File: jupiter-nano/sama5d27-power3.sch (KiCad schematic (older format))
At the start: 25 parts, among them U3 MIC5247-2.0YM5-TR

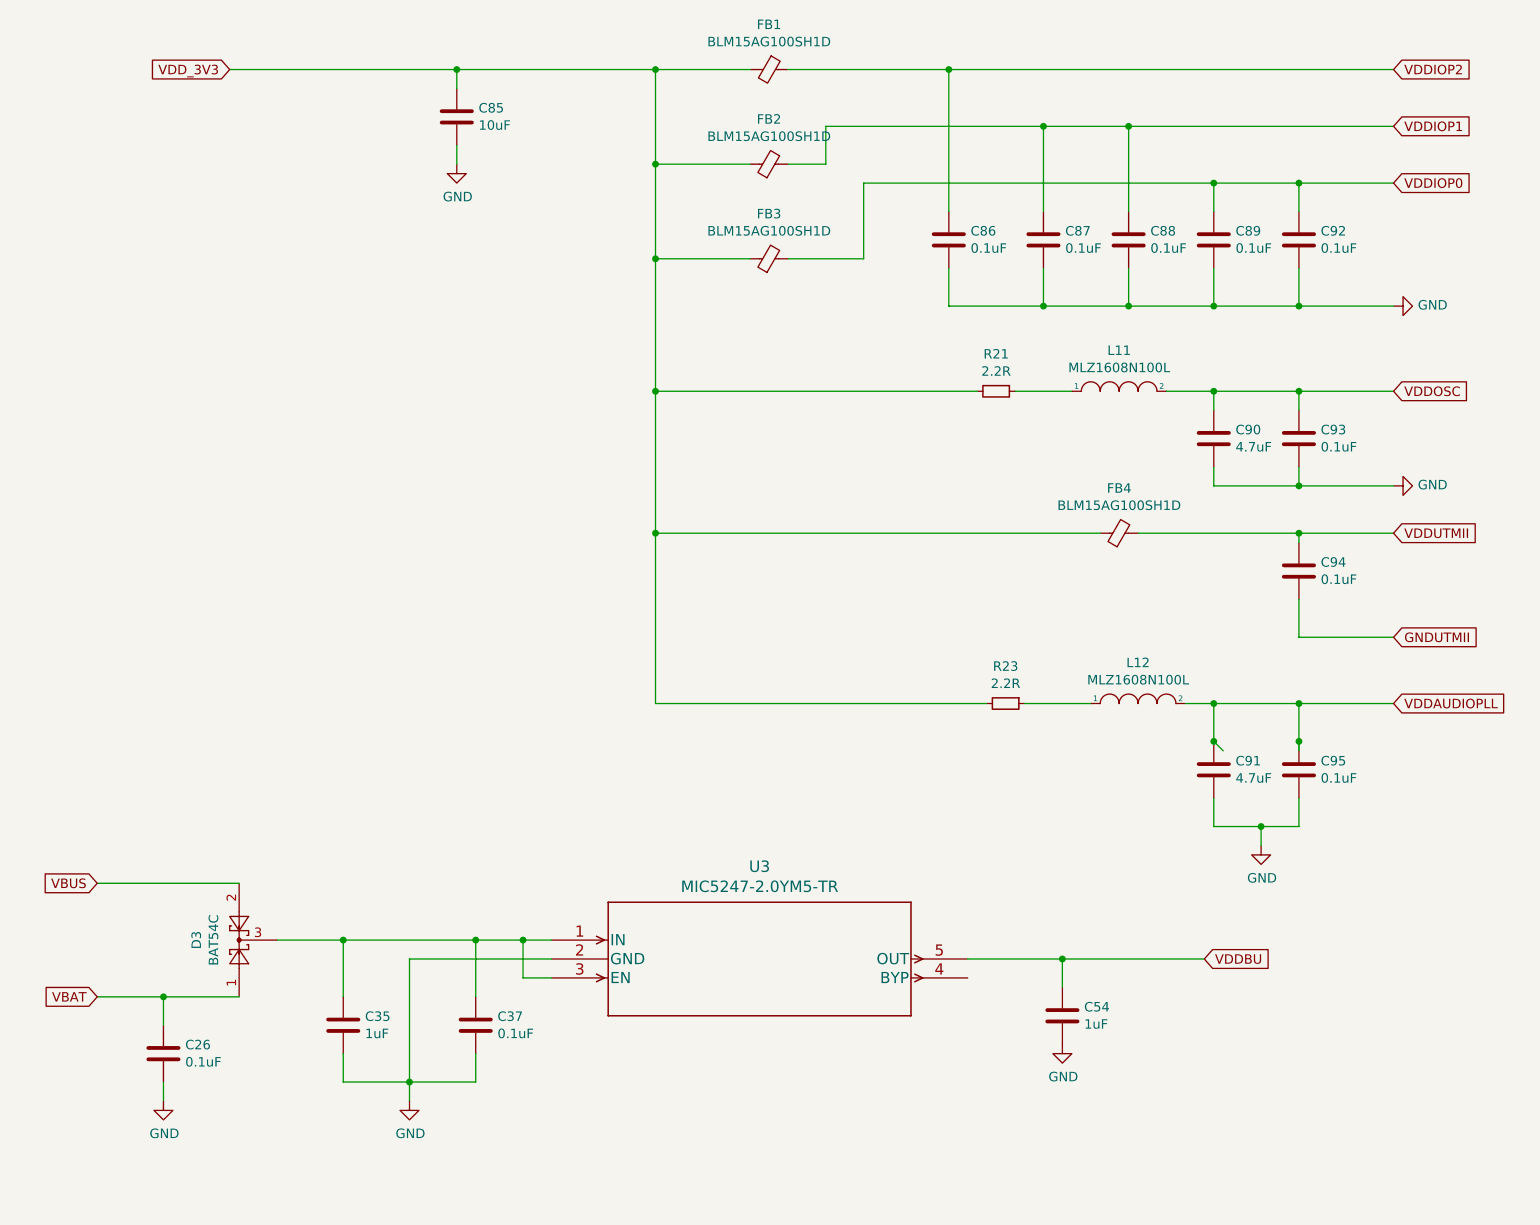
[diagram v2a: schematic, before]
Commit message: numerous ERC fixes
- still more to go
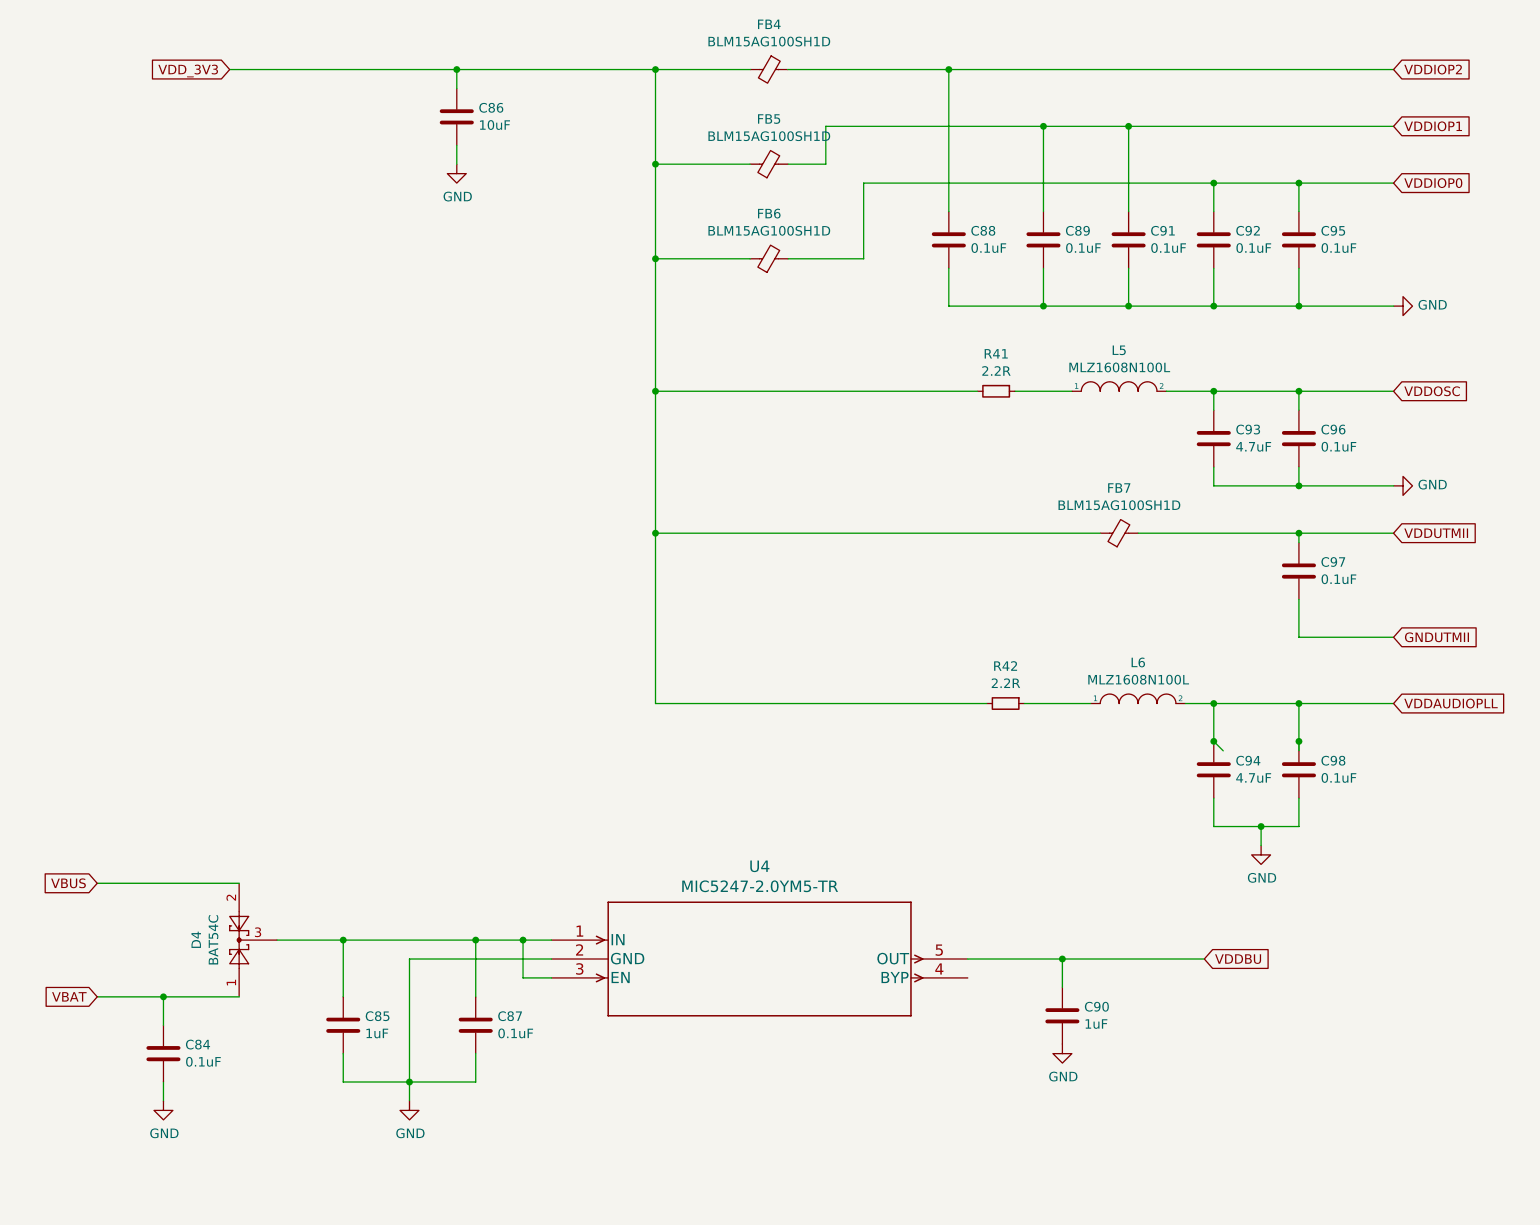
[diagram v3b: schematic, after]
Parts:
- renumbered C26 to C84, C35 to C85, C85 to C86, C37 to C87, C86 to C88, C87 to C89, C54 to C90, C88 to C91, C89 to C92, C90 to C93, C91 to C94, C92 to C95, C93 to C96, C94 to C97, C95 to C98, D3 to D4, FB1 to FB4, FB2 to FB5, FB3 to FB6, FB4 to FB7, L11 to L5, L12 to L6, R21 to R41, R23 to R42, U3 to U4
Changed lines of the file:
@@
 P 3850 5600
 AR Path="/5F395E67/5FD7EF72" Ref="U?"  Part="1"
-AR Path="/5FD740BF/5FD7EF72" Ref="U3"  Part="1"
-F 0 "U3" H 4950 5988 60  0000 C CNN
+AR Path="/5FD740BF/5FD7EF72" Ref="U4"  Part="1"
+F 0 "U4" H 4950 5988 60  0000 C CNN
 F 1 "MIC5247-2.0YM5-TR" H 4950 5882 60  0000 C CNN
 F 2 "SOT-23-5_M5_MCH" H 4950 5840 60  0001 C CNN
@@
 P 2200 5600
 AR Path="/5F395E67/5FD7EF78" Ref="D?"  Part="1"
-AR Path="/5FD740BF/5FD7EF78" Ref="D3"  Part="1"
-F 0 "D3" H 2200 5825 50  0000 C CNN
+AR Path="/5FD740BF/5FD7EF78" Ref="D4"  Part="1"
+F 0 "D4" H 2200 5825 50  0000 C CNN
 F 1 "BAT54C" H 2200 5734 50  0000 C CNN
 F 2 "Package_TO_SOT_SMD:SOT-23" H 2275 5725 50  0001 L CNN
@@
 $EndComp
 $Comp
-L Device:C C35
+L Device:C C85
 U 1 1 5FD81A7E
 P 2750 6050
-F 0 "C35" H 2865 6096 50  0000 L CNN
+F 0 "C85" H 2865 6096 50  0000 L CNN
 F 1 "1uF" H 2865 6005 50  0000 L CNN
 F 2 "Capacitor_SMD:C_0201_0603Metric" H 2788 5900 50  0001 C CNN
@@
 $EndComp
 $Comp
-L Device:C C26
+L Device:C C84
 U 1 1 5FD82B07
 P 1800 6200
-F 0 "C26" H 1915 6246 50  0000 L CNN
+F 0 "C84" H 1915 6246 50  0000 L CNN
 F 1 "0.1uF" H 1915 6155 50  0000 L CNN
 F 2 "Capacitor_SMD:C_0201_0603Metric" H 1838 6050 50  0001 C CNN
@@
 $EndComp
 $Comp
-L Device:C C37
+L Device:C C87
 U 1 1 5FD8300B
 P 3450 6050
-F 0 "C37" H 3565 6096 50  0000 L CNN
+F 0 "C87" H 3565 6096 50  0000 L CNN
 F 1 "0.1uF" H 3565 6005 50  0000 L CNN
 F 2 "Capacitor_SMD:C_0201_0603Metric" H 3488 5900 50  0001 C CNN
@@
 $EndComp
 $Comp
-L Device:C C54
+L Device:C C90
 U 1 1 5FD85AB1
 P 6550 6000
-F 0 "C54" H 6665 6046 50  0000 L CNN
+F 0 "C90" H 6665 6046 50  0000 L CNN
 F 1 "1uF" H 6665 5955 50  0000 L CNN
 F 2 "Capacitor_SMD:C_0201_0603Metric" H 6588 5850 50  0001 C CNN
@@
 P 5000 1000
 AR Path="/5F395E67/5FD936CB" Ref="FB?"  Part="1"
-AR Path="/5FD740BF/5FD936CB" Ref="FB1"  Part="1"
-F 0 "FB1" V 4763 1000 50  0000 C CNN
+AR Path="/5FD740BF/5FD936CB" Ref="FB4"  Part="1"
+F 0 "FB4" V 4763 1000 50  0000 C CNN
 F 1 "BLM15AG100SH1D" V 4854 1000 50  0000 C CNN
 F 2 "Capacitor_SMD:C_0402_1005Metric" V 4930 1000 50  0001 C CNN
@@
 P 5000 2000
 AR Path="/5F395E67/5FD936D1" Ref="FB?"  Part="1"
-AR Path="/5FD740BF/5FD936D1" Ref="FB3"  Part="1"
-F 0 "FB3" V 5237 2000 50  0000 C CNN
+AR Path="/5FD740BF/5FD936D1" Ref="FB6"  Part="1"
+F 0 "FB6" V 5237 2000 50  0000 C CNN
 F 1 "BLM15AG100SH1D" V 5146 2000 50  0000 C CNN
 F 2 "Capacitor_SMD:C_0402_1005Metric" V 4930 2000 50  0001 C CNN
@@
 P 5000 1500
 AR Path="/5F395E67/5FD936D7" Ref="FB?"  Part="1"
-AR Path="/5FD740BF/5FD936D7" Ref="FB2"  Part="1"
-F 0 "FB2" V 5237 1500 50  0000 C CNN
+AR Path="/5FD740BF/5FD936D7" Ref="FB5"  Part="1"
+F 0 "FB5" V 5237 1500 50  0000 C CNN
 F 1 "BLM15AG100SH1D" V 5146 1500 50  0000 C CNN
 F 2 "Capacitor_SMD:C_0402_1005Metric" V 4930 1500 50  0001 C CNN
@@
 	6550 5700 7300 5700
 $Comp
-L power:GND #PWR0168
+L power:GND #PWR072
 U 1 1 5FD98CB8
 P 6550 6150
-F 0 "#PWR0168" H 6550 5900 50  0001 C CNN
+F 0 "#PWR072" H 6550 5900 50  0001 C CNN
 F 1 "GND" H 6555 5977 50  0000 C CNN
 F 2 "" H 6550 6150 50  0001 C CNN
@@
 	3100 6350 3100 6450
 $Comp
-L power:GND #PWR0169
+L power:GND #PWR070
 U 1 1 5FD9D491
 P 3100 6450
-F 0 "#PWR0169" H 3100 6200 50  0001 C CNN
+F 0 "#PWR070" H 3100 6200 50  0001 C CNN
 F 1 "GND" H 3105 6277 50  0000 C CNN
 F 2 "" H 3100 6450 50  0001 C CNN
@@
 	1800 5900 1450 5900
 $Comp
-L power:GND #PWR0170
+L power:GND #PWR069
 U 1 1 5FDA258D
 P 1800 6450
-F 0 "#PWR0170" H 1800 6200 50  0001 C CNN
+F 0 "#PWR069" H 1800 6200 50  0001 C CNN
 F 1 "GND" H 1805 6277 50  0000 C CNN
 F 2 "" H 1800 6450 50  0001 C CNN
@@
 VDDAUDIOPLL
 $Comp
-L Device:C C92
+L Device:C C95
 U 1 1 5FDA6B92
 P 7800 1900
-F 0 "C92" H 7915 1946 50  0000 L CNN
+F 0 "C95" H 7915 1946 50  0000 L CNN
 F 1 "0.1uF" H 7915 1855 50  0000 L CNN
 F 2 "" H 7838 1750 50  0001 C CNN
@@
 $EndComp
 $Comp
-L Device:C C89
+L Device:C C92
 U 1 1 5FDA78C1
 P 7350 1900
-F 0 "C89" H 7465 1946 50  0000 L CNN
+F 0 "C92" H 7465 1946 50  0000 L CNN
 F 1 "0.1uF" H 7465 1855 50  0000 L CNN
 F 2 "" H 7388 1750 50  0001 C CNN
@@
 $EndComp
 $Comp
-L Device:C C88
+L Device:C C91
 U 1 1 5FDA7D34
 P 6900 1900
-F 0 "C88" H 7015 1946 50  0000 L CNN
+F 0 "C91" H 7015 1946 50  0000 L CNN
 F 1 "0.1uF" H 7015 1855 50  0000 L CNN
 F 2 "" H 6938 1750 50  0001 C CNN
@@
 $EndComp
 $Comp
-L Device:C C87
+L Device:C C89
 U 1 1 5FDA82B1
 P 6450 1900
-F 0 "C87" H 6565 1946 50  0000 L CNN
+F 0 "C89" H 6565 1946 50  0000 L CNN
 F 1 "0.1uF" H 6565 1855 50  0000 L CNN
 F 2 "" H 6488 1750 50  0001 C CNN
@@
 $EndComp
 $Comp
-L Device:C C86
+L Device:C C88
 U 1 1 5FDA8496
 P 5950 1900
-F 0 "C86" H 6065 1946 50  0000 L CNN
+F 0 "C88" H 6065 1946 50  0000 L CNN
 F 1 "0.1uF" H 6065 1855 50  0000 L CNN
 F 2 "" H 5988 1750 50  0001 C CNN
@@
 	5950 2250 6450 2250
 $Comp
-L power:GND #PWR0171
+L power:GND #PWR074
 U 1 1 5FDA8E26
 P 8300 2250
-F 0 "#PWR0171" H 8300 2000 50  0001 C CNN
+F 0 "#PWR074" H 8300 2000 50  0001 C CNN
 F 1 "GND" V 8305 2122 50  0000 R CNN
 F 2 "" H 8300 2250 50  0001 C CNN
@@
 P 6850 3450
 AR Path="/5F395E67/5FDB3C78" Ref="FB?"  Part="1"
-AR Path="/5FD740BF/5FDB3C78" Ref="FB4"  Part="1"
-F 0 "FB4" V 7087 3450 50  0000 C CNN
+AR Path="/5FD740BF/5FDB3C78" Ref="FB7"  Part="1"
+F 0 "FB7" V 7087 3450 50  0000 C CNN
 F 1 "BLM15AG100SH1D" V 6996 3450 50  0000 C CNN
 F 2 "Capacitor_SMD:C_0402_1005Metric" V 6780 3450 50  0001 C CNN
@@
 $EndComp
 $Comp
-L Device:C C93
+L Device:C C96
 U 1 1 5FDC0270
 P 7800 2950
-F 0 "C93" H 7915 2996 50  0000 L CNN
+F 0 "C96" H 7915 2996 50  0000 L CNN
 F 1 "0.1uF" H 7915 2905 50  0000 L CNN
 F 2 "" H 7838 2800 50  0001 C CNN
@@
 $EndComp
 $Comp
-L Device:C C90
+L Device:C C93
 U 1 1 5FDC0F33
 P 7350 2950
-F 0 "C90" H 7465 2996 50  0000 L CNN
+F 0 "C93" H 7465 2996 50  0000 L CNN
 F 1 "4.7uF" H 7465 2905 50  0000 L CNN
 F 2 "" H 7388 2800 50  0001 C CNN
@@
 $EndComp
 $Comp
-L Device:C C94
+L Device:C C97
 U 1 1 5FDC11E1
 P 7800 3650
-F 0 "C94" H 7915 3696 50  0000 L CNN
+F 0 "C97" H 7915 3696 50  0000 L CNN
 F 1 "0.1uF" H 7915 3605 50  0000 L CNN
 F 2 "" H 7838 3500 50  0001 C CNN
@@
 $EndComp
 $Comp
-L Device:C C95
+L Device:C C98
 U 1 1 5FDC1F0D
 P 7800 4700
-F 0 "C95" H 7915 4746 50  0000 L CNN
+F 0 "C98" H 7915 4746 50  0000 L CNN
 F 1 "0.1uF" H 7915 4655 50  0000 L CNN
 F 2 "" H 7838 4550 50  0001 C CNN
@@
 $EndComp
 $Comp
-L Device:C C91
+L Device:C C94
 U 1 1 5FDC275A
 P 7350 4700
-F 0 "C91" H 7465 4746 50  0000 L CNN
+F 0 "C94" H 7465 4746 50  0000 L CNN
 F 1 "4.7uF" H 7465 4655 50  0000 L CNN
 F 2 "" H 7388 4550 50  0001 C CNN
@@
 	7600 5000 7800 5000
 $Comp
-L power:GND #PWR0172
+L power:GND #PWR073
 U 1 1 5FE0FC03
 P 7600 5100
-F 0 "#PWR0172" H 7600 4850 50  0001 C CNN
+F 0 "#PWR073" H 7600 4850 50  0001 C CNN
 F 1 "GND" H 7605 4927 50  0000 C CNN
 F 2 "" H 7600 5100 50  0001 C CNN
@@
 	7800 3200 8300 3200
 $Comp
-L power:GND #PWR0173
+L power:GND #PWR075
 U 1 1 5FE13F3A
 P 8300 3200
-F 0 "#PWR0173" H 8300 2950 50  0001 C CNN
+F 0 "#PWR075" H 8300 2950 50  0001 C CNN
 F 1 "GND" V 8305 3072 50  0000 R CNN
 F 2 "" H 8300 3200 50  0001 C CNN
@@
 	7350 2700 7350 2800
 $Comp
-L pspice:INDUCTOR L11
+L pspice:INDUCTOR L5
 U 1 1 5FE20C65
 P 6850 2700
-F 0 "L11" H 6850 2915 50  0000 C CNN
+F 0 "L5" H 6850 2915 50  0000 C CNN
 F 1 "MLZ1608N100L" H 6850 2824 50  0000 C CNN
 F 2 "Capacitor_SMD:C_0603_1608Metric" H 6850 2700 50  0001 C CNN
@@
 $EndComp
 $Comp
-L Device:R_Small R21
+L Device:R_Small R41
 U 1 1 5FE21466
 P 6200 2700
-F 0 "R21" V 6004 2700 50  0000 C CNN
+F 0 "R41" V 6004 2700 50  0000 C CNN
 F 1 "2.2R" V 6095 2700 50  0000 C CNN
 F 2 "" H 6200 2700 50  0001 C CNN
@@
 VDD_3V3
 $Comp
-L Device:C C85
+L Device:C C86
 U 1 1 5FE45547
 P 3350 1250
-F 0 "C85" H 3465 1296 50  0000 L CNN
+F 0 "C86" H 3465 1296 50  0000 L CNN
 F 1 "10uF" H 3465 1205 50  0000 L CNN
 F 2 "" H 3388 1100 50  0001 C CNN
@@
 	3350 1400 3350 1500
 $Comp
-L power:GND #PWR0174
+L power:GND #PWR071
 U 1 1 5FE4A1D6
 P 3350 1500
-F 0 "#PWR0174" H 3350 1250 50  0001 C CNN
+F 0 "#PWR071" H 3350 1250 50  0001 C CNN
 F 1 "GND" H 3355 1327 50  0000 C CNN
 F 2 "" H 3350 1500 50  0001 C CNN
@@
 $EndComp
 $Comp
-L pspice:INDUCTOR L12
+L pspice:INDUCTOR L6
 U 1 1 5FE4ABBC
 P 6950 4350
-F 0 "L12" H 6950 4565 50  0000 C CNN
+F 0 "L6" H 6950 4565 50  0000 C CNN
 F 1 "MLZ1608N100L" H 6950 4474 50  0000 C CNN
 F 2 "Capacitor_SMD:C_0603_1608Metric_Pad1.05x0.95mm_HandSolder" H 6950 4350 50  0001 C CNN
@@
 $EndComp
 $Comp
-L Device:R_Small R23
+L Device:R_Small R42
 U 1 1 5FE4B82E
 P 6250 4350
-F 0 "R23" V 6054 4350 50  0000 C CNN
+F 0 "R42" V 6054 4350 50  0000 C CNN
 F 1 "2.2R" V 6145 4350 50  0000 C CNN
 F 2 "" H 6250 4350 50  0001 C CNN
